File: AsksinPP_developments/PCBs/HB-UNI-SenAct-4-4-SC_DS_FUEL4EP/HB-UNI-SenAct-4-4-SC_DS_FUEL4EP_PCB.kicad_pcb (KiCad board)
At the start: 2 copper layers, 86 x 63 mm, 53 parts, among them J1 5V supply, J10 charge, J2 4x Push Buttons, J3 4x Relais, J4 5x LEDs, J5 ISP Programmer, J6 Accumulator, J7 GND, J8 VCC, Q1 IRLU024N, Q2 BD238, Q4 IRF9Z34N, Q5 MCP1702-2802E_TO, SW1 SW_Push, SW2 SW_Push

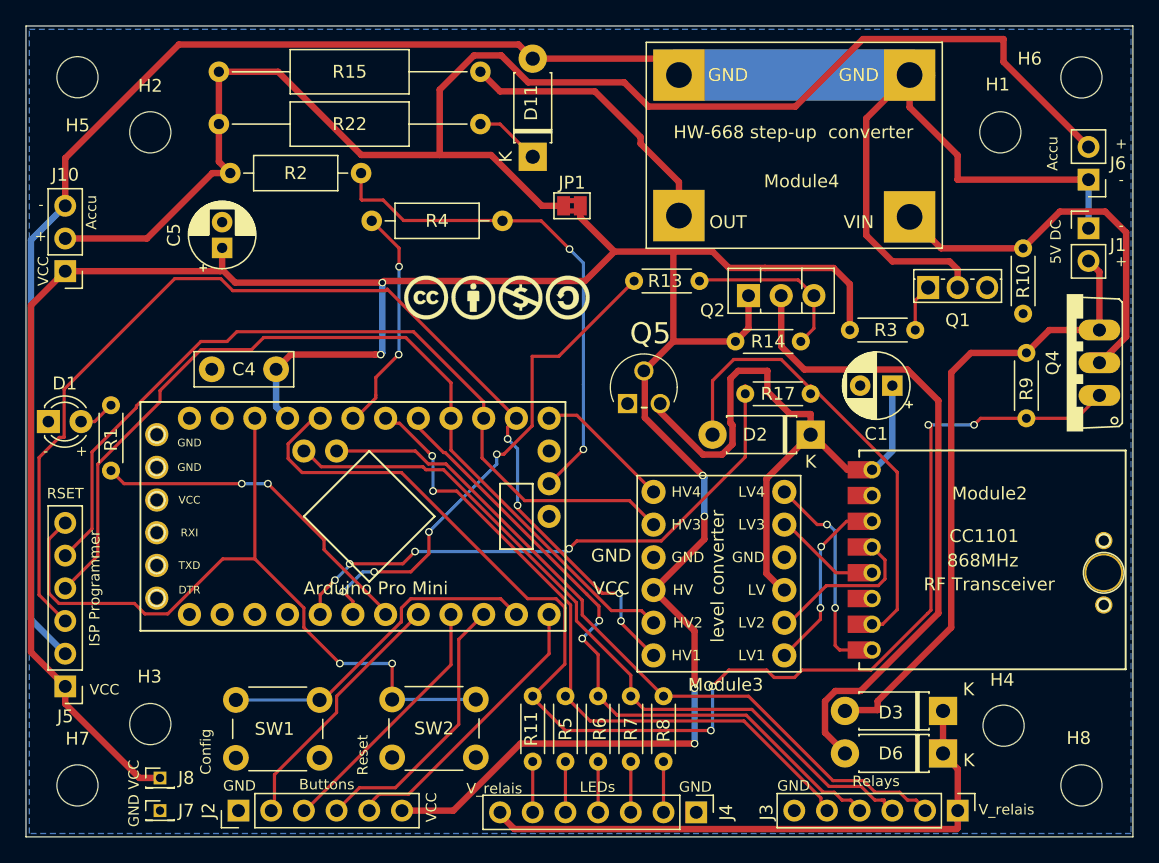
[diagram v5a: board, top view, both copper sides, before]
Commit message: PCBs: KiCAD6 required improvements of layout data bases; added E07-900M10S into FUEL and footprint library
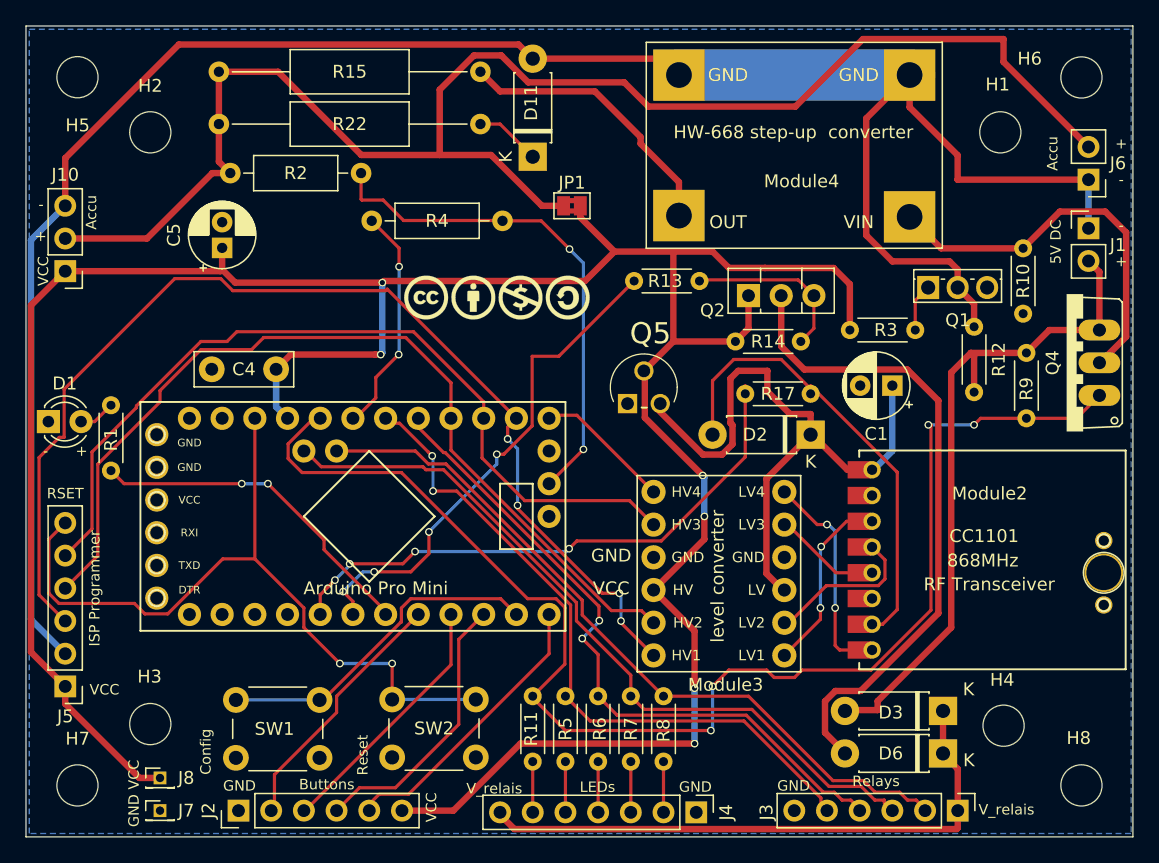
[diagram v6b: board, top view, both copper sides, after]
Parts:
- added R12: 4.7k, Resistor_THT:R_Axial_DIN0204_L3.6mm_D1.6mm_P5.08mm_Horizontal, F.Cu at (73.7, 23.4)
- Module4: value HW-668_step-up -> HW-668_step_up
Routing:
- net /V_supply: track 49.4 -> 52.6 mm
- net /minusBAT: track 158.0 -> 159.8 mm
- net /A0: track 52.6 -> 51.9 mm
- net /D9: track 22.4 -> 21.9 mm
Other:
- board text added: "(C) FUEL4EP 07/2023 triple power switch for 230V demand switch zero standby power (only accumulators) V1.5"
- board text removed: "(C) FUEL4EP 06/2023 triple power switch for 230V demand switch zero standby power (only accumulators) V1.3"
